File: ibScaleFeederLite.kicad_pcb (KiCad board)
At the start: 4 copper layers, 51.6 x 89 mm, 89 parts, among them J1 PEEL, J2 DRIVE, J3 RAIL, J4 SWD, J5 Serial, J6 SWD, SW1 DOWN, SW2 UP, SW3 BOOT, U2 DRV8837, U3 DRV8837, U4 THVD1400D, U5 TPS563300, U6 AMS1117-3.3, U9 STM32F031C6Tx, Y1 8MHz

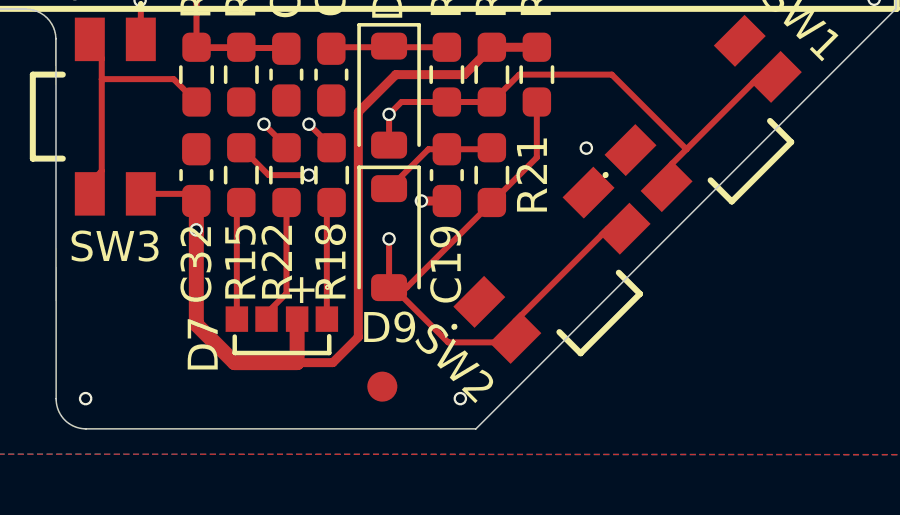
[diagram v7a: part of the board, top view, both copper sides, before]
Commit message: Change VDDA ferrite to 120-ohm for better parts availability
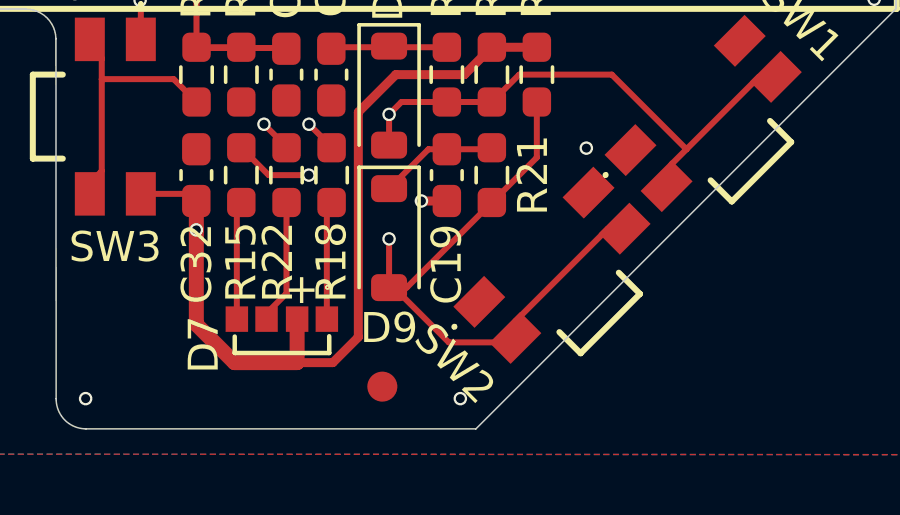
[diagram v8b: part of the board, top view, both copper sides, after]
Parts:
- L2: value 100r -> 120r
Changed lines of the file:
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@@
 			)
 		)
-		(property "Value" "100r"
+		(property "Value" "120r"
 			(at 0 1.43 0)
 			(layer "F.Fab")
@@
 			)
 		)
-		(property "Manufacturer_Name" "TDK"
+		(property "Manufacturer_Name" "Eaton"
 			(at 0 0 180)
 			(unlocked yes)
@@
 			)
 		)
-		(property "LCSC" "C501996"
+		(property "LCSC" "C14709"
 			(at 0 0 180)
 			(unlocked yes)
@@
 			)
 		)
-		(property "Mouser" "810-MPZ1608Y101BTA00"
+		(property "Mouser" "704-MFBM1V1608-121-R"
 			(at 0 0 180)
 			(unlocked yes)
@@
 			)
 		)
-		(property "Manufacturer_Part" "MPZ1608Y101BTA00"
+		(property "Manufacturer_Part" "MFBM1V1608-121-R"
 			(at 0 0 180)
 			(unlocked yes)
@@
 			)
 		)
-		(property "DigiKey" "445-MPZ1608Y101BTA00CT-ND"
+		(property "DigiKey" "283-MFBM1V1608-121-RCT-ND"
 			(at 0 0 180)
 			(unlocked yes)
@@
 			)
 		)
+		(property "Tolerance" ""
+			(at 0 0 270)
+			(unlocked yes)
+			(layer "F.Fab")
+			(hide yes)
+			(effects
+				(font
+					(size 1 1)
+					(thickness 0.15)
+				)
+			)
+		)
+		(property "Rating" ""
+			(at 0 0 270)
+			(unlocked yes)
+			(layer "F.Fab")
+			(hide yes)
+			(effects
+				(font
+					(size 1 1)
+					(thickness 0.15)
+				)
+			)
+		)
+		(property "Notes" ""
+			(at 0 0 270)
+			(unlocked yes)
+			(layer "F.Fab")
+			(hide yes)
+			(effects
+				(font
+					(size 1 1)
+					(thickness 0.15)
+				)
+			)
+		)
 		(property ki_fp_filters "R_*")
 		(sheetname "/")
@@
 	)
 	(segment
-		(start 129.7125 110.25)
-		(end 132.55 107.4125)
+		(start 129.290618 110.25)
+		(end 131.115618 112.075)
 		(width 0.2)
 		(layer "F.Cu")
@@
 	)
 	(segment
-		(start 131.093569 112.075)
-		(end 133.18627 112.075)
+		(start 133.18627 112.075)
+		(end 133.334835 111.926435)
 		(width 0.2)
 		(layer "F.Cu")
@@
 	)
 	(segment
-		(start 129.268569 110.25)
-		(end 131.093569 112.075)
+		(start 129.7125 110.25)
+		(end 132.55 107.4125)
+		(width 0.2)
+		(layer "F.Cu")
+		(net "/SW_UP")
+	)
+	(segment
+		(start 131.115618 112.075)
+		(end 133.18627 112.075)
 		(width 0.2)
 		(layer "F.Cu")
@@
 	)
 	(segment
-		(start 133.18627 112.075)
-		(end 133.334835 111.926435)
+		(start 129.125 110.25)
+		(end 129.290618 110.25)
 		(width 0.2)
 		(layer "F.Cu")
@@
 		(width 0.2)
 		(layer "F.Cu")
-		(net "/SW_UP")
-	)
-	(segment
-		(start 129.125 110.25)
-		(end 129.268569 110.25)
-		(width 0.2)
-		(layer "F.Cu")
